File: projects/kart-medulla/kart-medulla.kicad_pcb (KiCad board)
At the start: 2 copper layers, 68 x 60 mm, 57 parts, among them CN1 1990012, CN2 1990012, CN3 1990012, CN4 1990012, CN5 1990012, CN6 1990012, CN7 1990012, CN8 1990012, Q3 IRLZ44NPBF, Q4 BSS123_C5184436, U13 MCP4922-E/SL, U14 MAX4660EUA+T, U19 L7805CDT_C20611927, U23 SSW-122-01-T-D, U24 SSW-122-01-T-S, U25 PCF8574T/3,518, U4 LM358DR, U5 SN74LVC3G17DCTR

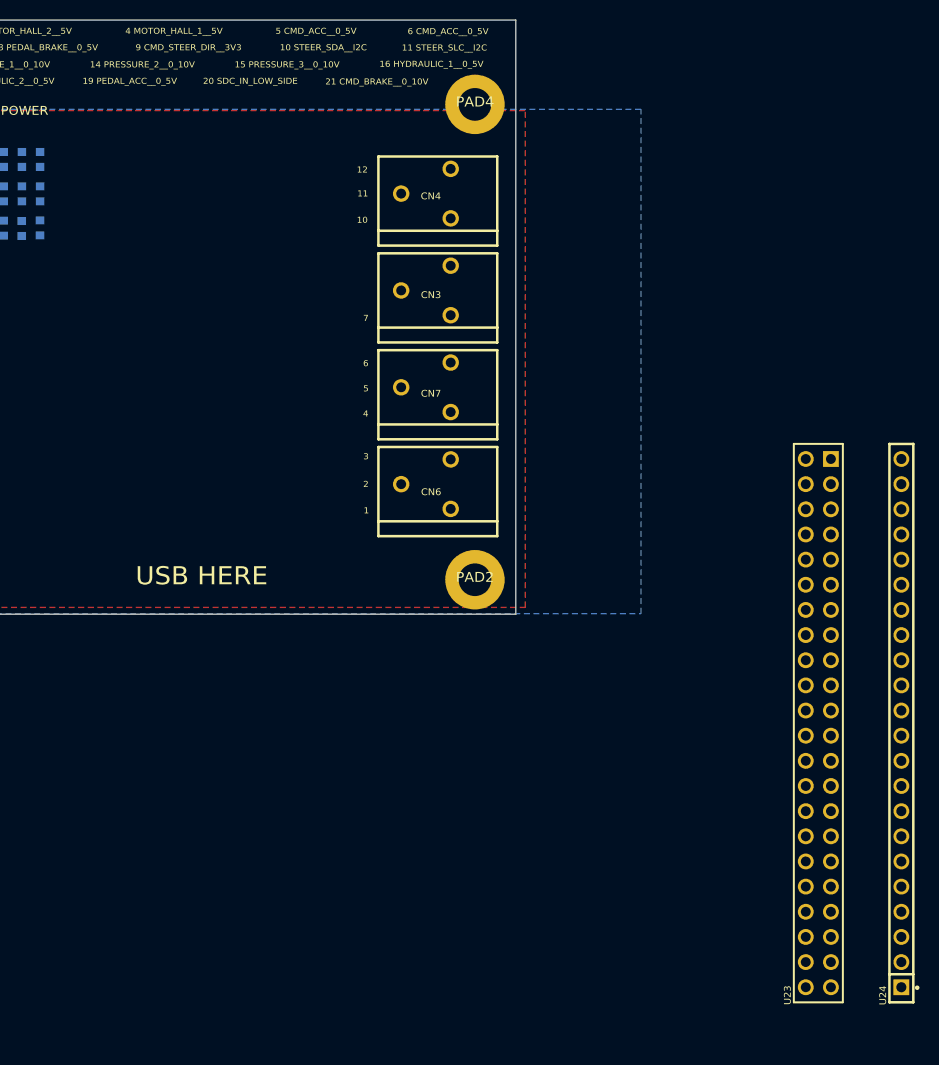
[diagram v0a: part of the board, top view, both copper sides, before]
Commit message: pcb headers lock
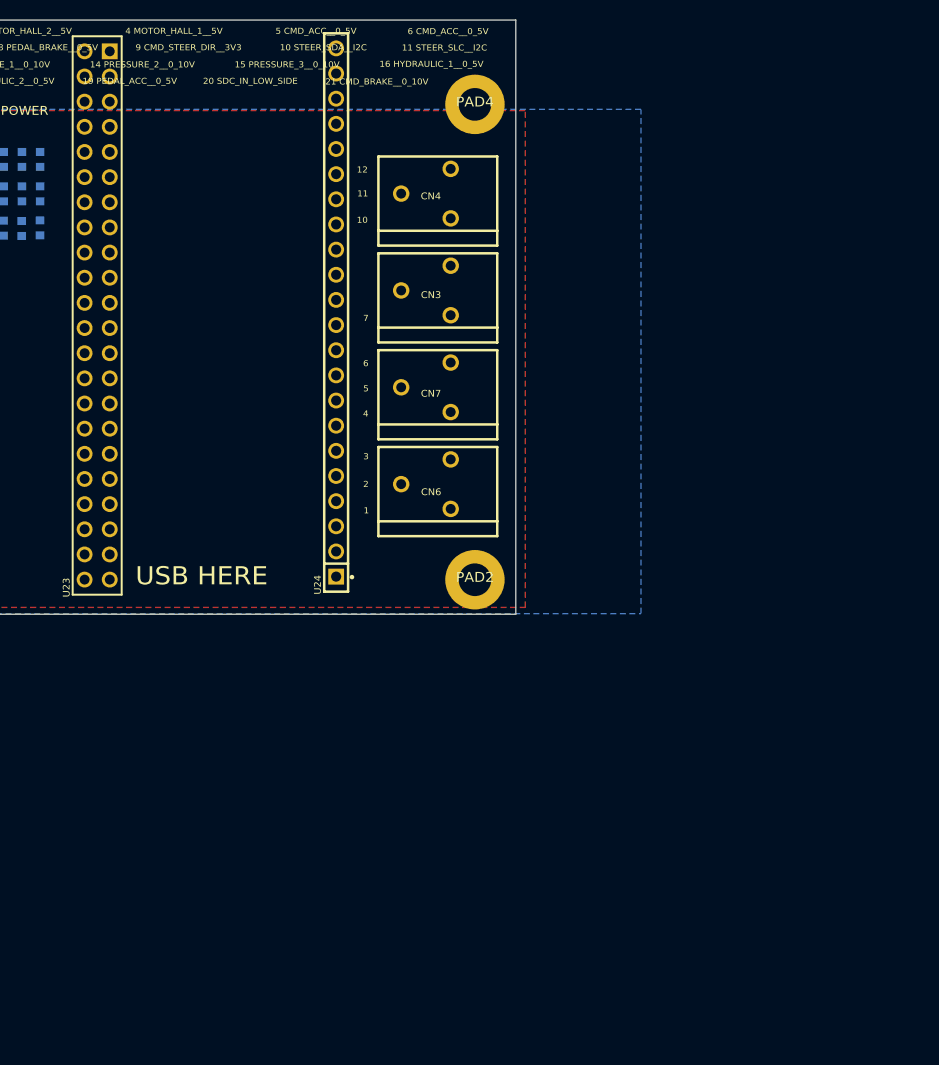
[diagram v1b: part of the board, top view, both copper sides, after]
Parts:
- moved U23 83.7 mm to (96.7, 73.8)
- moved U24 70.5 mm to (120.9, 73.5)
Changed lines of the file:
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@@
 	)
 	(footprint "HDR-TH_ESQ-122-59-G-D"
+		(locked yes)
 		(layer "F.Cu")
-		(at 169.5516 114.9931 90)
+		(at 96.73 73.83 90)
 		(property "Reference" "U23"
 			(at -28.4665 -2.702 90)
@@
 	)
 	(footprint "HDR-TH_ESQ-122-23-G-S"
+		(locked yes)
 		(layer "F.Cu")
-		(at 177.9336 114.9931 90)
+		(at 120.86 73.53 90)
 		(property "Reference" "U24"
 			(at -28.4884 -1.459 90)

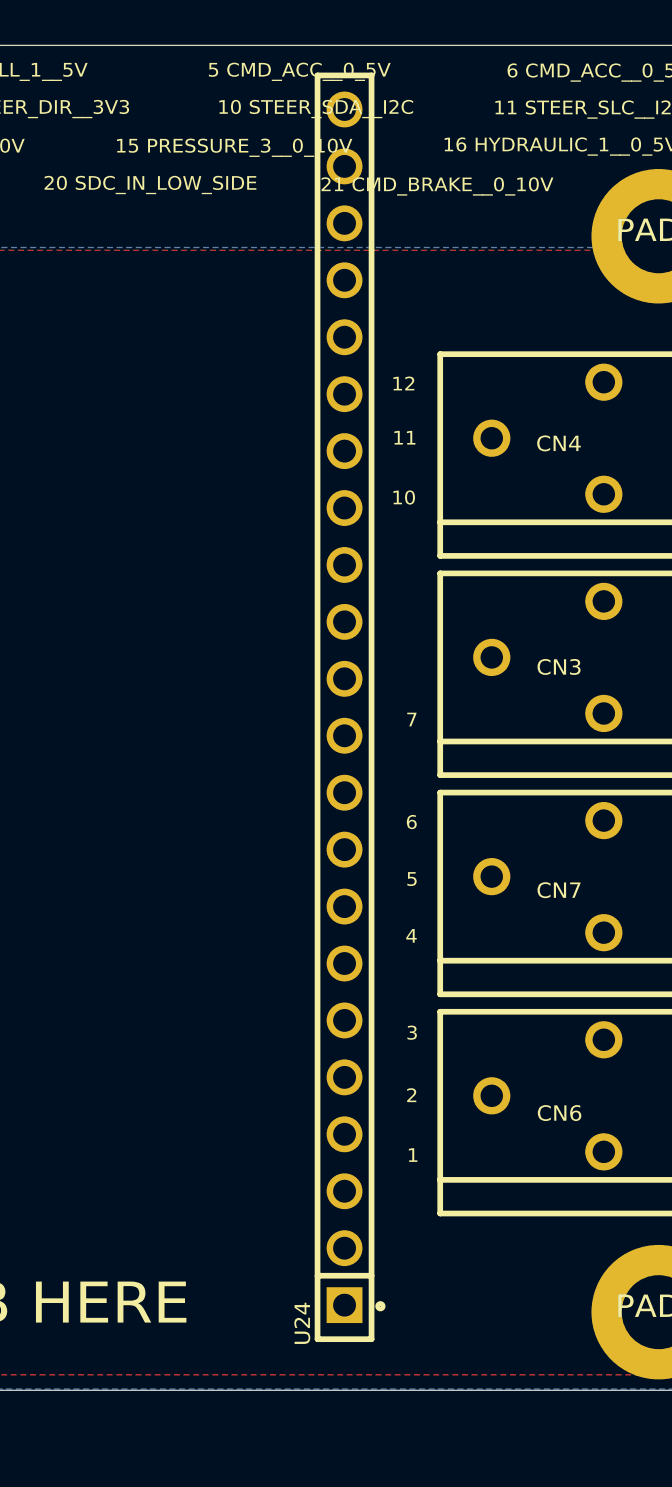
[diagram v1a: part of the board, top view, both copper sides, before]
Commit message: headers lock update
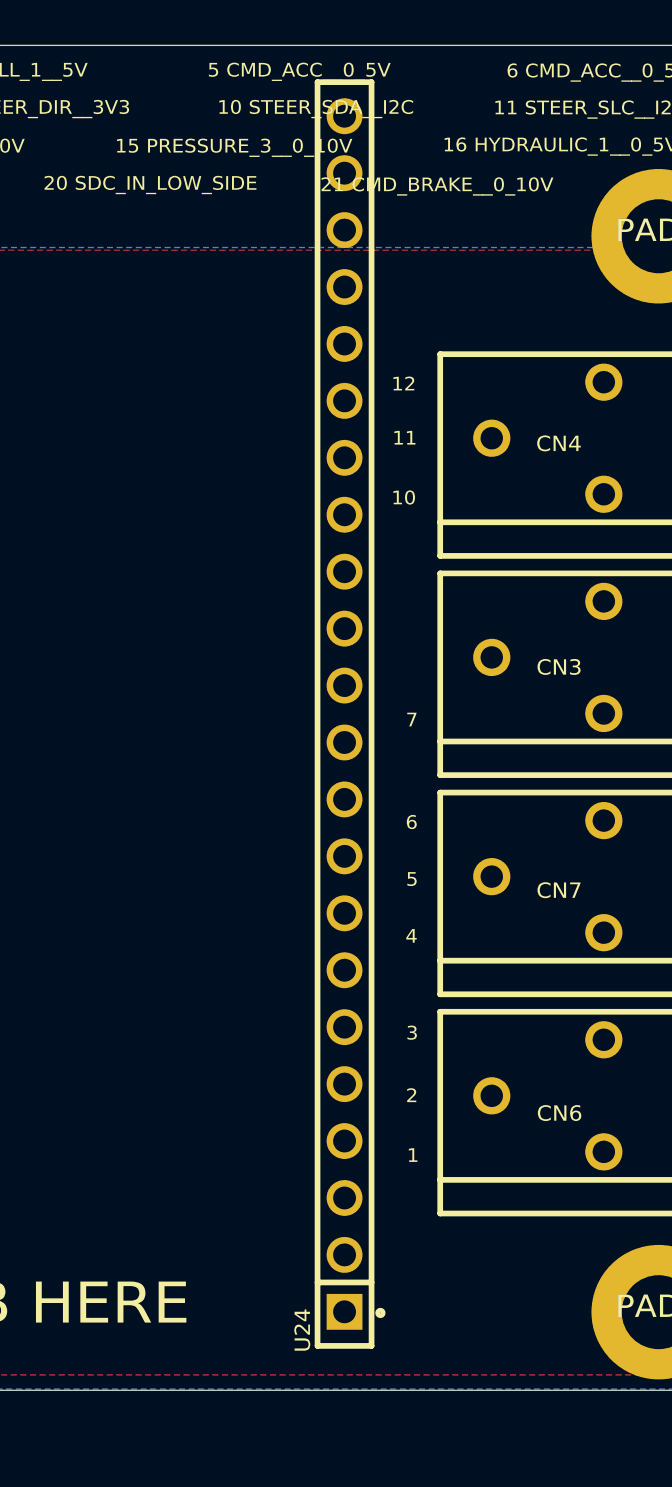
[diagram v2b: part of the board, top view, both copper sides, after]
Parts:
- moved U24 0.30 mm to (120.9, 73.8)
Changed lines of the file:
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@@
 		(locked yes)
 		(layer "F.Cu")
-		(at 120.86 73.53 90)
+		(at 120.86 73.83 90)
 		(property "Reference" "U24"
 			(at -28.4884 -1.459 90)
